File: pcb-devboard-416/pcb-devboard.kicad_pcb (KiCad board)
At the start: 2 copper layers, 52.5 x 49.9 mm, 28 parts, among them J1 UPDI_PROGRAMMER, J2 PINS1, J3 PINS2, J4 PINS1, J5 PINS1, U1 CH340E, U2 ATtiny412-SS

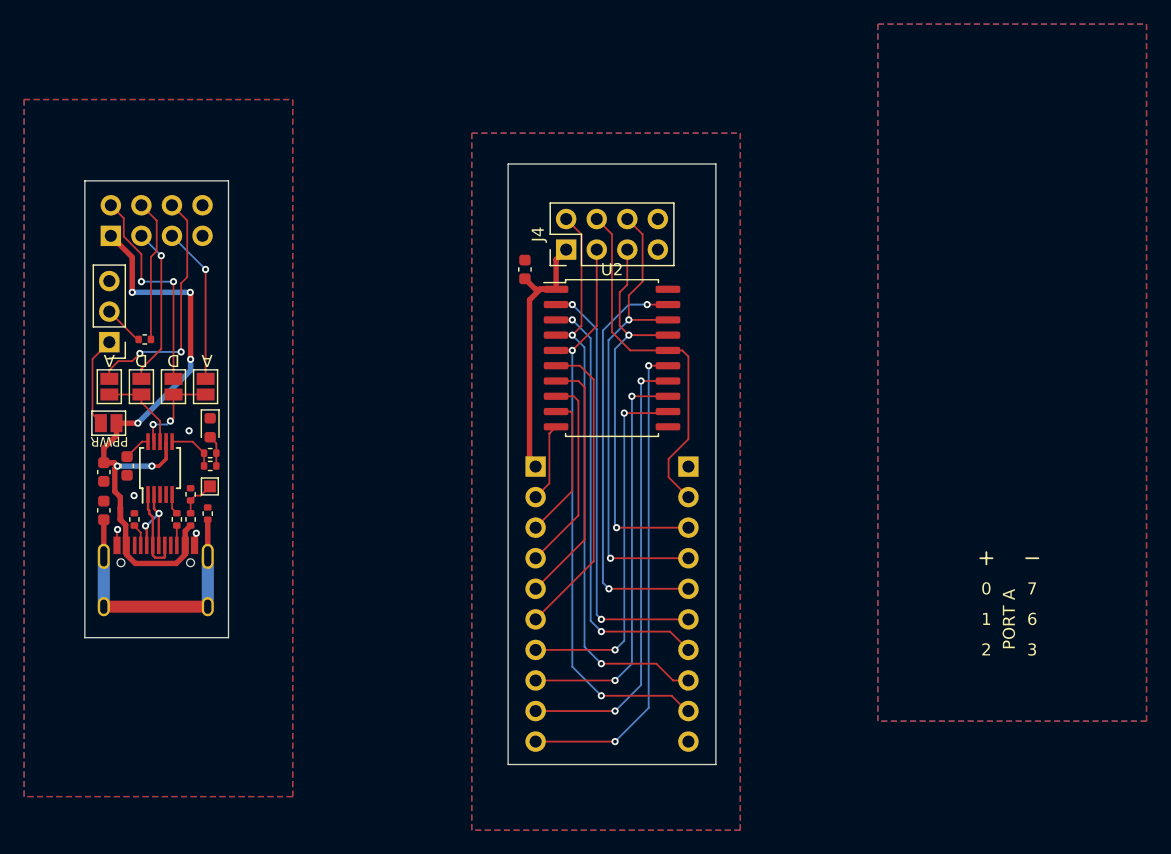
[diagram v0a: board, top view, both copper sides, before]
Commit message: 416 dev board: Version 1.0 as manufactured
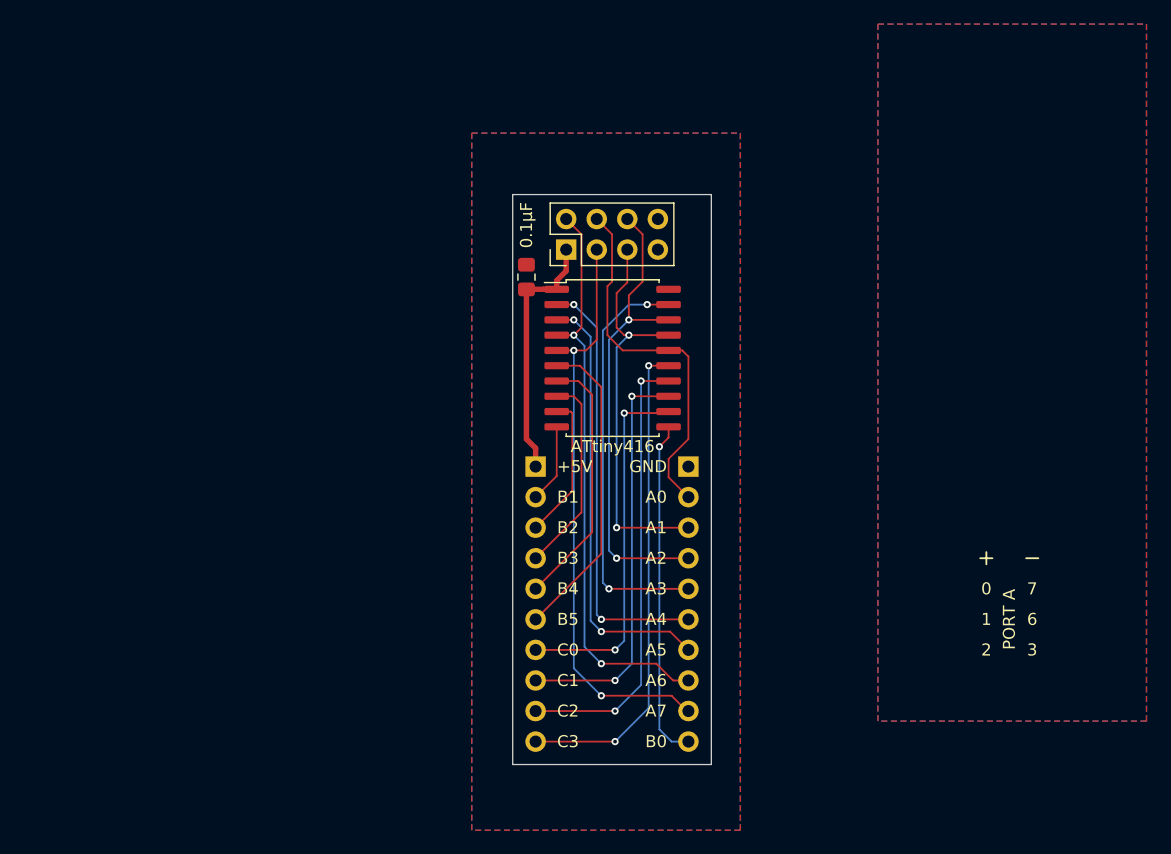
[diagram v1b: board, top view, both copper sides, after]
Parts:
- removed C1, C2, C4: 0.1μF, Capacitor_SMD:C_0603_1608Metric
- removed D1: LED, LED_SMD:LED_0603_1608Metric
- removed J1: UPDI_PROGRAMMER, Connector_PinHeader_2.54mm:PinHeader_1x03_P2.54mm_Vertical
- removed J5: PINS1, Connector_PinSocket_2.54mm:PinSocket_2x04_P2.54mm_Vertical
- removed JP1, JP2, JP3, JP4, JP5: SolderJumper_2_Open, Jumper:SolderJumper-2_P1.3mm_Open_Pad1.0x1.5mm
- removed NT1: NetTie_2, NetTie:NetTie-2_SMD_Pad0.5mm
- removed R1, R2, R6, R7, R8: 5.1K 0402, Resistor_SMD:R_0402_1005Metric
- removed R3: 220 0402, Resistor_SMD:R_0402_1005Metric
- removed R4: 5.6K 0402, Resistor_SMD:R_0402_1005Metric
- removed R5: 10k, Resistor_SMD:R_0402_1005Metric
- removed TP1: TestPoint, mine:TestPoint_Pad_1.0x1.0mm
- removed U1: CH340E, Package_SO:MSOP-10_3x3mm_P0.5mm
- removed USB1: TYPE-C-31-M-12, HRO:HRO-TYPE-C-31-M-12
- C3: footprint Capacitor_SMD:C_0603_1608Metric -> mine:my_C_0805_2012Metric_Pad1.15x1.40mm_HandSolder
- U2: value ATtiny412-SS -> ATtiny416
- moved C3 0.65 mm to (105.9, 96.0)
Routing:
- net VSYS: track 60.6 -> 21.1 mm, vias 6 -> 0
- net /PIN_PB0: track 0.00 -> 28.3 mm, vias 0 -> 1
- net Net-(C1-Pad2): track 23.1 -> 0.00 mm
- net /PIN_PA2: track 60.0 -> 39.4 mm, vias 4 -> 2
- net /PIN_PA6: track 66.1 -> 48.0 mm, vias 4 -> 2
- net /PIN_PA1: track 46.5 -> 33.8 mm, vias 3 -> 2
- net /PIN_PA7: track 61.2 -> 48.5 mm, vias 3 -> 2
- net /PIN_PA0: track 42.0 -> 30.9 mm
- net /VBUS: track 11.1 -> 0.00 mm
- net /USB_UART_RX: track 7.88 -> 0.00 mm, vias 2 -> 0
- net /USB_D-: track 7.60 -> 0.00 mm, vias 2 -> 0
- net Net-(J1-Pad1): track 7.53 -> 0.00 mm
- net /USB_D+: track 7.28 -> 0.00 mm
- net /USB_UART_TX: track 7.23 -> 0.00 mm
- net GND: track 4.12 -> 0.00 mm, vias 4 -> 0
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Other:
- board size 52.5 x 49.9 mm -> 16.5 x 47.4 mm
- board text added: "+5V"
- board text added: "A0"
- board text added: "A1"
- board text added: "A2"
- board text added: "A3"
- board text added: "A4"
- board text added: "A5"
- board text added: "A6"
- board text added: "A7"
- board text added: "B0"
- board text added: "B1"
- board text added: "B2"
- board text added: "B3"
- board text added: "B4"
- board text added: "B5"
- board text added: "C0"
- board text added: "C1"
- board text added: "C2"
- board text added: "C3"
- board text added: "GND"
- board text added: "by Tarn"
- board text removed: "A"
- board text removed: "D"
- board text removed: "PPWR"

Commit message: 41x interface board: Version 1.1 as manufactured
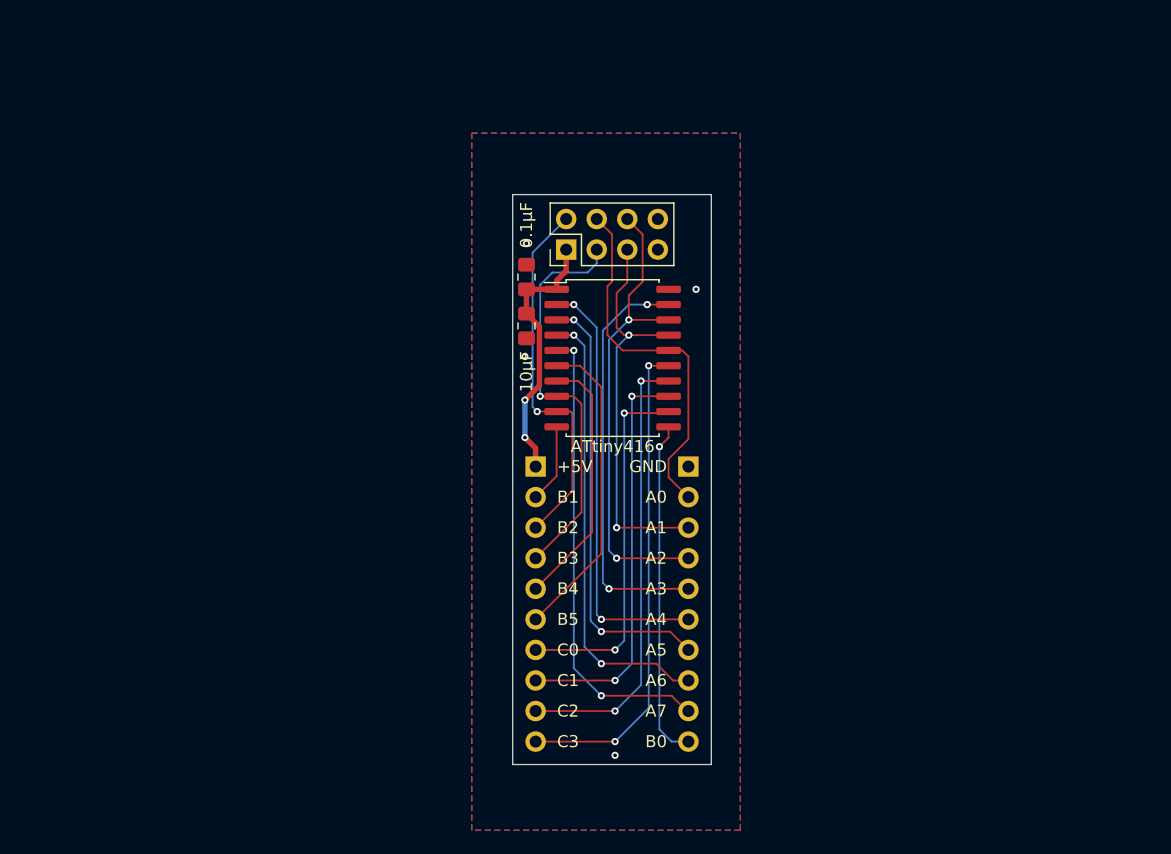
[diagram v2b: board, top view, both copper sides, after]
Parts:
- added C1: 10μF, mine:my_C_0805_2012Metric_Pad1.15x1.40mm_HandSolder, F.Cu at (105.9, 100.1)
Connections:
- J4 pad 2: /PIN_PA6 -> /PIN_PB2
- J4 pad 3: /PIN_PA7 -> /PIN_PB3
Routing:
- net /PIN_PB2: track 12.2 -> 31.1 mm, vias 0 -> 1
- net /PIN_PB3: track 16.8 -> 34.0 mm, vias 0 -> 1
- net /PIN_PA6: track 48.0 -> 37.5 mm
- net /PIN_PA7: track 48.5 -> 38.8 mm
- net VSYS: track 21.1 -> 22.1 mm, vias 0 -> 2
- net GND: vias 0 -> 4
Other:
- board text added: "JLCJLCJLCJLC"
- board text added: "v1.1 by Tarn"
- board text removed: "0"
- board text removed: "1"
- board text removed: "2"
- board text removed: "3"
- board text removed: "6"
- board text removed: "7"
- board text removed: "PORT A"
- board text removed: "by Tarn"
